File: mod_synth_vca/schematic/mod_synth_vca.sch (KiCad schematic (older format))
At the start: 46 parts, among them J1 Conn_02x08_Odd_Even, J2 AudioJack2, J3 AudioJack2, J4 AudioJack2, J5 AudioJack2, J6 AudioJack2, J7 AudioJack2, J8 Conn_01x10_Female, J9 Conn_01x10_Male, U1 TL074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

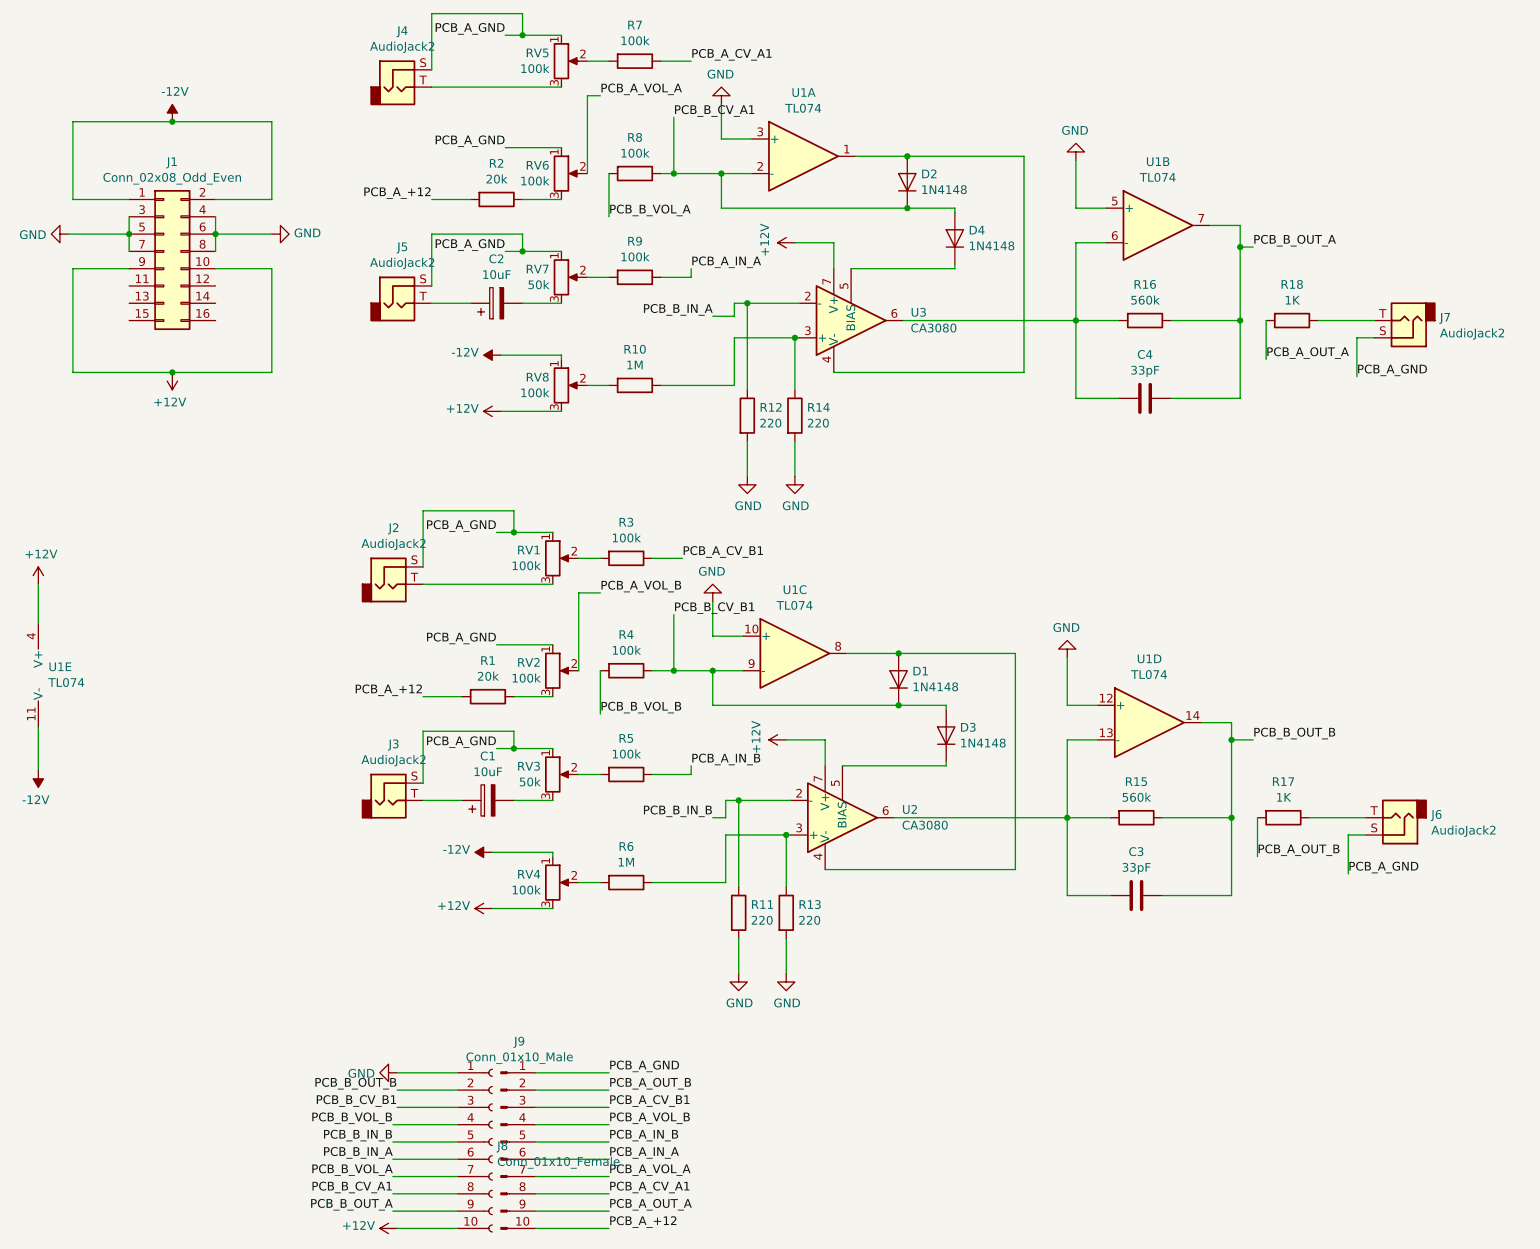
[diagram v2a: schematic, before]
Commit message: Alter PCB layouts
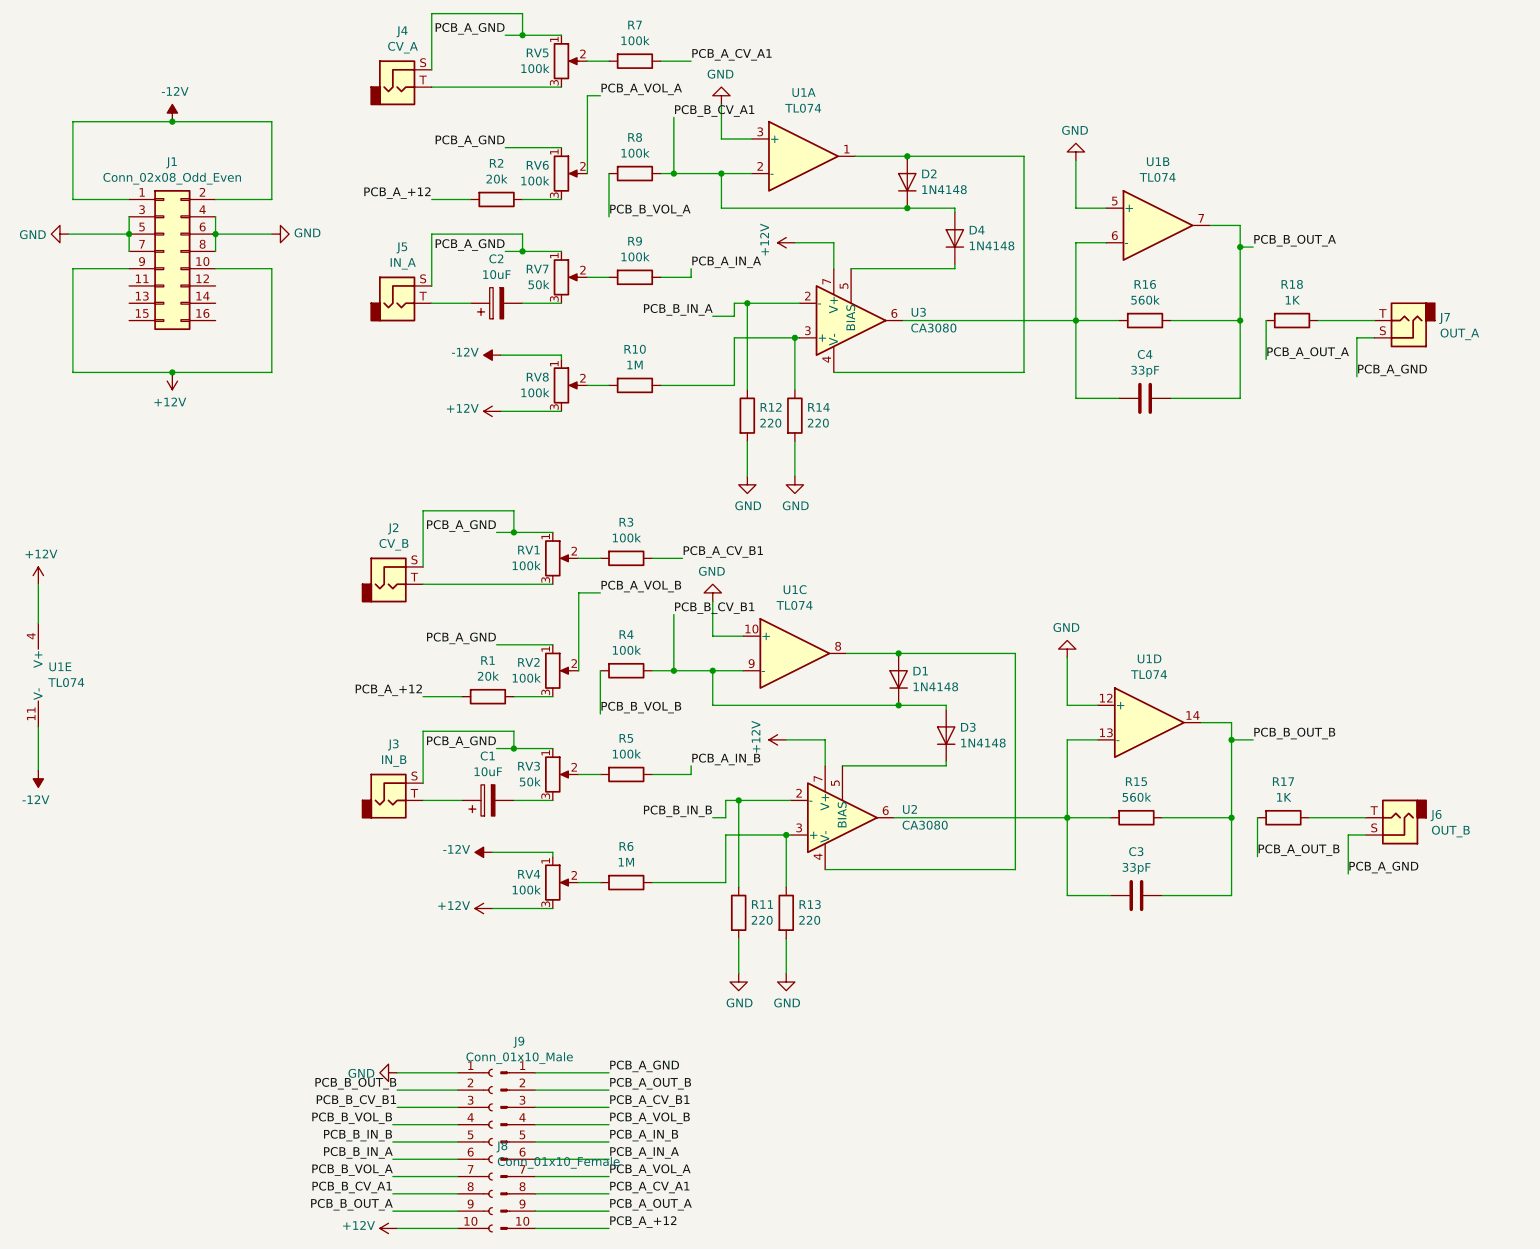
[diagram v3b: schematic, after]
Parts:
- J2: value AudioJack2 -> CV_B
- J3: value AudioJack2 -> IN_B
- J4: value AudioJack2 -> CV_A
- J5: value AudioJack2 -> IN_A
- J6: value AudioJack2 -> OUT_B
- J7: value AudioJack2 -> OUT_A
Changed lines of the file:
@@
 P 3300 1050
 F 0 "J4" H 3332 1375 50  0000 C CNN
-F 1 "AudioJack2" H 3332 1284 50  0000 C CNN
+F 1 "CV_A" H 3332 1284 50  0000 C CNN
 F 2 "Connector_Audio:Jack_3.5mm_QingPu_WQP-PJ398SM_Vertical_CircularHoles" H 3300 1050 50  0001 C CNN
 F 3 "~" H 3300 1050 50  0001 C CNN
@@
 P 3300 2300
 F 0 "J5" H 3332 2625 50  0000 C CNN
-F 1 "AudioJack2" H 3332 2534 50  0000 C CNN
+F 1 "IN_A" H 3332 2534 50  0000 C CNN
 F 2 "Connector_Audio:Jack_3.5mm_QingPu_WQP-PJ398SM_Vertical_CircularHoles" H 3300 2300 50  0001 C CNN
 F 3 "~" H 3300 2300 50  0001 C CNN
@@
 P 9150 2400
 F 0 "J7" H 8970 2383 50  0000 R CNN
-F 1 "AudioJack2" H 8970 2474 50  0000 R CNN
+F 1 "OUT_A" H 8970 2474 50  0000 R CNN
 F 2 "Connector_Audio:Jack_3.5mm_QingPu_WQP-PJ398SM_Vertical_CircularHoles" H 9150 2400 50  0001 C CNN
 F 3 "~" H 9150 2400 50  0001 C CNN
@@
 P 3250 3925
 F 0 "J2" H 3282 4250 50  0000 C CNN
-F 1 "AudioJack2" H 3282 4159 50  0000 C CNN
+F 1 "CV_B" H 3282 4159 50  0000 C CNN
 F 2 "Connector_Audio:Jack_3.5mm_QingPu_WQP-PJ398SM_Vertical_CircularHoles" H 3250 3925 50  0001 C CNN
 F 3 "~" H 3250 3925 50  0001 C CNN
@@
 P 3250 5175
 F 0 "J3" H 3282 5500 50  0000 C CNN
-F 1 "AudioJack2" H 3282 5409 50  0000 C CNN
+F 1 "IN_B" H 3282 5409 50  0000 C CNN
 F 2 "Connector_Audio:Jack_3.5mm_QingPu_WQP-PJ398SM_Vertical_CircularHoles" H 3250 5175 50  0001 C CNN
 F 3 "~" H 3250 5175 50  0001 C CNN
@@
 P 9100 5275
 F 0 "J6" H 8920 5258 50  0000 R CNN
-F 1 "AudioJack2" H 8920 5349 50  0000 R CNN
+F 1 "OUT_B" H 8920 5349 50  0000 R CNN
 F 2 "Connector_Audio:Jack_3.5mm_QingPu_WQP-PJ398SM_Vertical_CircularHoles" H 9100 5275 50  0001 C CNN
 F 3 "~" H 9100 5275 50  0001 C CNN
